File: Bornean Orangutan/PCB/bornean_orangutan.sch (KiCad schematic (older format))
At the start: 1 part

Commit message: Update Bornean Orangutan-Schematic & -PCB
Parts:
- added C1, C2: 22pF, Capacitor_SMD:C_0805_2012Metric, symbol Device:C_Small
- added C3, C4, C5, C6: 0.1uF, Capacitor_SMD:C_0805_2012Metric, symbol Device:C_Small
- added D1, D10, D11, D12, D13, D14, D15, D16, D17, D18, D19, D2, D20, D21, D22, D23, D24, D25, D3, D4, D5, D6, D7, D8, D9: SOD-123, Diode_SMD:D_SOD-123, symbol Device:D_Small
- added EXTRADATA1: Extradata, Connector_Pin:Pin_D1.0mm_L10.0mm, symbol Connector_Generic:Conn_01x01
- added F1: 500mA, Fuse:Fuse_1206_3216Metric, symbol Device:Fuse_Small
- added J1, J2: TRRS, Connector_Audio:Jack_3.5mm_PJ320D_Horizontal, symbol Connector:AudioJack3_Ground
- added MX1, MX10, MX11, MX12, MX13, MX14, MX15, MX16, MX17, MX18, MX19, MX2, MX20, MX21, MX22, MX23, MX24, MX25, MX3, MX4, MX5, MX6, MX7, MX8, MX9: MX-NoLED, MX_Alps_Hybrid:MX-1U, symbol MX_Alps_Hybrid:MX-NoLED
- added R1, R4: 10k, Resistor_SMD:R_0805_2012Metric, symbol Device:R_Small
- added R2, R3: 22, Resistor_SMD:R_0805_2012Metric, symbol Device:R_Small
- added SW1: SW_Push, random-keyboard-parts:SKQG-1155865, symbol Switch:SW_Push
- added USB1: Molex-0548190589, random-keyboard-parts:Molex-0548190589, symbol random-keyboard-parts:Molex-0548190589
- added Y1: 16MHz, Crystal:Crystal_SMD_3225-4Pin_3.2x2.5mm, symbol Device:Crystal_GND24_Small
- gave numbers to parts that had none: 1
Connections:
- net +5V: now also U1.7 (VBUS), C3.1, C4.1, C5.1, C6.1, F1.2, R1.1
- net GND: now also C1.2, C2.2, C3.2, C4.2, C5.2, C6.2, J1.G, J2.G, R4.1, SW1.1, USB1.1 (GND), Y1.2, Y1.4
- net COL1: now reaches U1.10 (PB2)
- net COL1: now also MX12.1 (COL), MX17.1 (COL), MX2.1 (COL), MX22.1 (COL), MX7.1 (COL)
- net COL2: now reaches U1.11 (PB3)
- net COL2: now also MX13.1 (COL), MX18.1 (COL), MX23.1 (COL), MX3.1 (COL), MX8.1 (COL)
- net at U1.13 (~RESET): now also R1.2, SW1.2
- net at U1.16 (XTAL2): now also C2.1, Y1.3
- net at U1.17 (XTAL1): now also C1.1, Y1.1
- net COL3: now reaches U1.21 (PD3)
- net COL3: now also MX14.1 (COL), MX19.1 (COL), MX24.1 (COL), MX4.1 (COL), MX9.1 (COL)
- net COL4: now reaches U1.22 (PD5)
- net COL4: now also MX10.1 (COL), MX15.1 (COL), MX20.1 (COL), MX25.1 (COL), MX5.1 (COL)
- net at U1.3 (D-): now also R3.1
- net at U1.33 (~HWB~/PE2): now also R4.2
- net ROW0: now reaches U1.37 (PF6)
- net ROW0: now also D1.1 (K), D2.1 (K), D3.1 (K), D4.1 (K), D5.1 (K)
- net ROW1: now reaches U1.38 (PF5)
- net ROW1: now also D10.1 (K), D6.1 (K), D7.1 (K), D8.1 (K), D9.1 (K)
- net ROW2: now reaches U1.39 (PF4)
- net ROW2: now also D11.1 (K), D12.1 (K), D13.1 (K), D14.1 (K), D15.1 (K)
- net at U1.4 (D+): now also R2.1
- net ROW3: now reaches U1.40 (PF1)
- net ROW3: now also D16.1 (K), D17.1 (K), D18.1 (K), D19.1 (K), D20.1 (K)
- net ROW4: now reaches U1.41 (PF0)
- net ROW4: now also D21.1 (K), D22.1 (K), D23.1 (K), D24.1 (K), D25.1 (K)
- net at U1.8 (PB0): now also J1.T, J2.T
- net COL0: now reaches U1.9 (PB1)
- net COL0: now also MX1.1 (COL), MX11.1 (COL), MX16.1 (COL), MX21.1 (COL), MX6.1 (COL)
- new net: EXTRADATA1.1 (Pin_1), J1.S, J2.S
- new net: D1.2 (A), MX1.2 (ROW)
- new net: D2.2 (A), MX2.2 (ROW)
- new net: D3.2 (A), MX3.2 (ROW)
- new net: D4.2 (A), MX4.2 (ROW)
- new net: D5.2 (A), MX5.2 (ROW)
- new net: D6.2 (A), MX6.2 (ROW)
- new net: D7.2 (A), MX7.2 (ROW)
- new net: D8.2 (A), MX8.2 (ROW)
- new net: D9.2 (A), MX9.2 (ROW)
- new net: D10.2 (A), MX10.2 (ROW)
- new net: D11.2 (A), MX11.2 (ROW)
- new net: D12.2 (A), MX12.2 (ROW)
- new net: D13.2 (A), MX13.2 (ROW)
- new net: D14.2 (A), MX14.2 (ROW)
- new net: D15.2 (A), MX15.2 (ROW)
- new net: D16.2 (A), MX16.2 (ROW)
- new net: D17.2 (A), MX17.2 (ROW)
- new net: D18.2 (A), MX18.2 (ROW)
- new net: D19.2 (A), MX19.2 (ROW)
- new net: D20.2 (A), MX20.2 (ROW)
- new net: D21.2 (A), MX21.2 (ROW)
- new net: D22.2 (A), MX22.2 (ROW)
- new net: D23.2 (A), MX23.2 (ROW)
- new net: D24.2 (A), MX24.2 (ROW)
- new net: D25.2 (A), MX25.2 (ROW)
- new net D+: R2.2, USB1.3 (D+)
- new net D-: R3.2, USB1.4 (D-)
- new net VCC: F1.1, J1.R, J2.R, USB1.5 (VBUS)
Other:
- moved on the sheet: U1

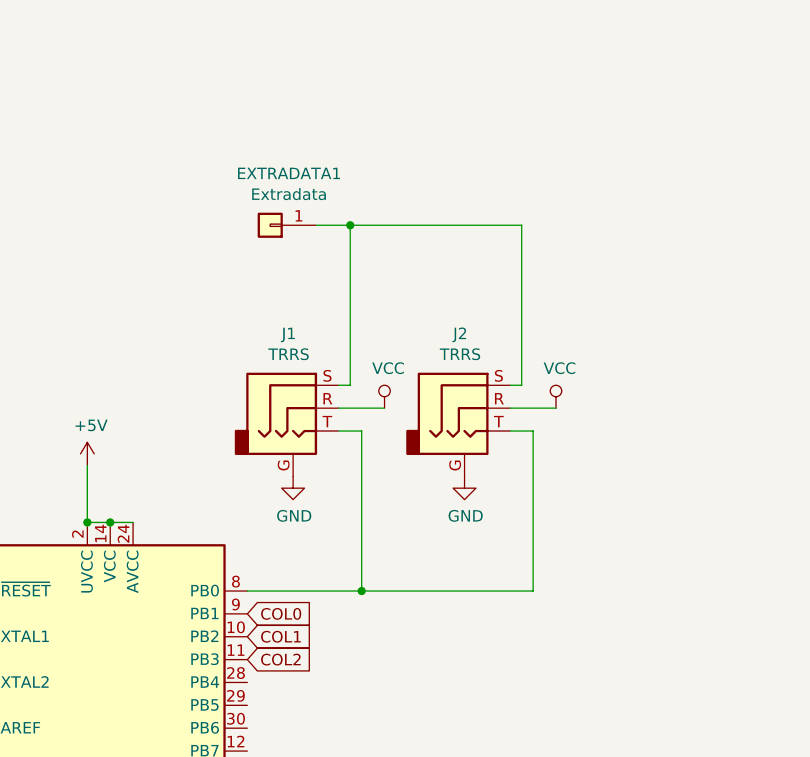
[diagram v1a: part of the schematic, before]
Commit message: Delete Tracks on Bornean Orangutan-PCB
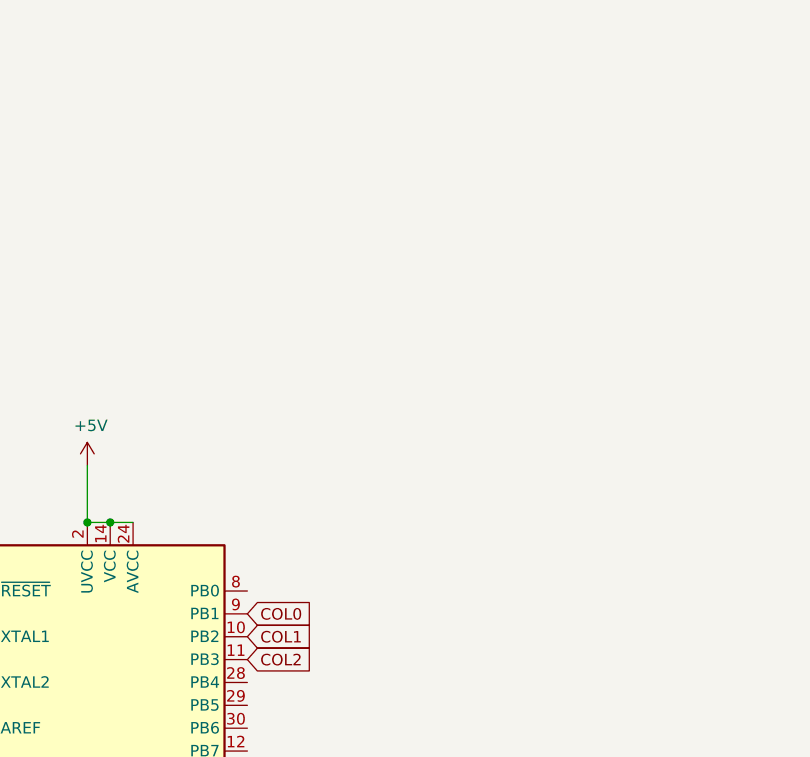
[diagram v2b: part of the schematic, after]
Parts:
- removed EXTRADATA1: Extradata, Connector_Pin:Pin_D1.0mm_L10.0mm, symbol Connector_Generic:Conn_01x01
- removed J1, J2: TRRS, Connector_Audio:Jack_3.5mm_PJ320D_Horizontal, symbol Connector:AudioJack3_Ground
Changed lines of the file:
@@
 Text GLabel 4050 4950 2    50   Input ~ 0
 COL4
-$Comp
-L Connector:AudioJack3_Ground J1
-U 1 1 5F35A7CD
-P 4250 2450
-F 0 "J1" H 4232 2775 50  0000 C CNN
-F 1 "TRRS" H 4232 2684 50  0000 C CNN
-F 2 "Connector_Audio:Jack_3.5mm_PJ320D_Horizontal" H 4250 2450 50  0001 C CNN
-F 3 "~" H 4250 2450 50  0001 C CNN
-	1    4250 2450
-	1    0    0    -1
-$EndComp
-$Comp
-L power:GND #PWR0113
-U 1 1 5F35BA3A
-P 4250 2750
-F 0 "#PWR0113" H 4250 2500 50  0001 C CNN
-F 1 "GND" H 4255 2577 50  0000 C CNN
-F 2 "" H 4250 2750 50  0001 C CNN
-F 3 "" H 4250 2750 50  0001 C CNN
-	1    4250 2750
-	1    0    0    -1
-$EndComp
-$Comp
-L Connector:AudioJack3_Ground J2
-U 1 1 5F38B226
-P 5000 2450
-F 0 "J2" H 4982 2775 50  0000 C CNN
-F 1 "TRRS" H 4982 2684 50  0000 C CNN
-F 2 "Connector_Audio:Jack_3.5mm_PJ320D_Horizontal" H 5000 2450 50  0001 C CNN
-F 3 "~" H 5000 2450 50  0001 C CNN
-	1    5000 2450
-	1    0    0    -1
-$EndComp
-$Comp
-L power:GND #PWR0114
-U 1 1 5F38B22C
-P 5000 2750
-F 0 "#PWR0114" H 5000 2500 50  0001 C CNN
-F 1 "GND" H 5005 2577 50  0000 C CNN
-F 2 "" H 5000 2750 50  0001 C CNN
-F 3 "" H 5000 2750 50  0001 C CNN
-	1    5000 2750
-	1    0    0    -1
-$EndComp
-Wire Wire Line
-	4450 2450 4650 2450
-$Comp
-L power:VCC #PWR0115
-U 1 1 5F393B94
-P 4650 2450
-F 0 "#PWR0115" H 4650 2300 50  0001 C CNN
-F 1 "VCC" H 4667 2623 50  0000 C CNN
-F 2 "" H 4650 2450 50  0001 C CNN
-F 3 "" H 4650 2450 50  0001 C CNN
-	1    4650 2450
-	1    0    0    -1
-$EndComp
-Wire Wire Line
-	5200 2450 5400 2450
-$Comp
-L power:VCC #PWR0116
-U 1 1 5F394588
-P 5400 2450
-F 0 "#PWR0116" H 5400 2300 50  0001 C CNN
-F 1 "VCC" H 5417 2623 50  0000 C CNN
-F 2 "" H 5400 2450 50  0001 C CNN
-F 3 "" H 5400 2450 50  0001 C CNN
-	1    5400 2450
-	1    0    0    -1
-$EndComp
-Wire Wire Line
-	4500 2350 4450 2350
-$Comp
-L Connector_Generic:Conn_01x01 EXTRADATA1
-U 1 1 5F398C08
-P 4150 1650
-F 0 "EXTRADATA1" H 4068 1425 50  0000 C CNN
-F 1 "Extradata" H 4068 1516 50  0000 C CNN
-F 2 "Connector_Pin:Pin_D1.0mm_L10.0mm" H 4150 1650 50  0001 C CNN
-F 3 "~" H 4150 1650 50  0001 C CNN
-	1    4150 1650
-	-1   0    0    1
-$EndComp
-Wire Wire Line
-	4500 1650 4500 2350
-Connection ~ 4500 1650
-Wire Wire Line
-	4500 1650 4350 1650
-Wire Wire Line
-	4050 3250 4550 3250
-Wire Wire Line
-	5300 3250 5300 2550
-Wire Wire Line
-	5300 2550 5200 2550
-Wire Wire Line
-	4450 2550 4550 2550
-Wire Wire Line
-	4550 2550 4550 3250
-Connection ~ 4550 3250
-Wire Wire Line
-	4550 3250 5300 3250
-Wire Wire Line
-	5250 1650 5250 2350
-Wire Wire Line
-	5250 2350 5200 2350
-Wire Wire Line
-	4500 1650 5250 1650
 $EndSCHEMATC
